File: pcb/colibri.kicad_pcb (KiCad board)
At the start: 2 copper layers, 160 x 94.7 mm, 91 parts

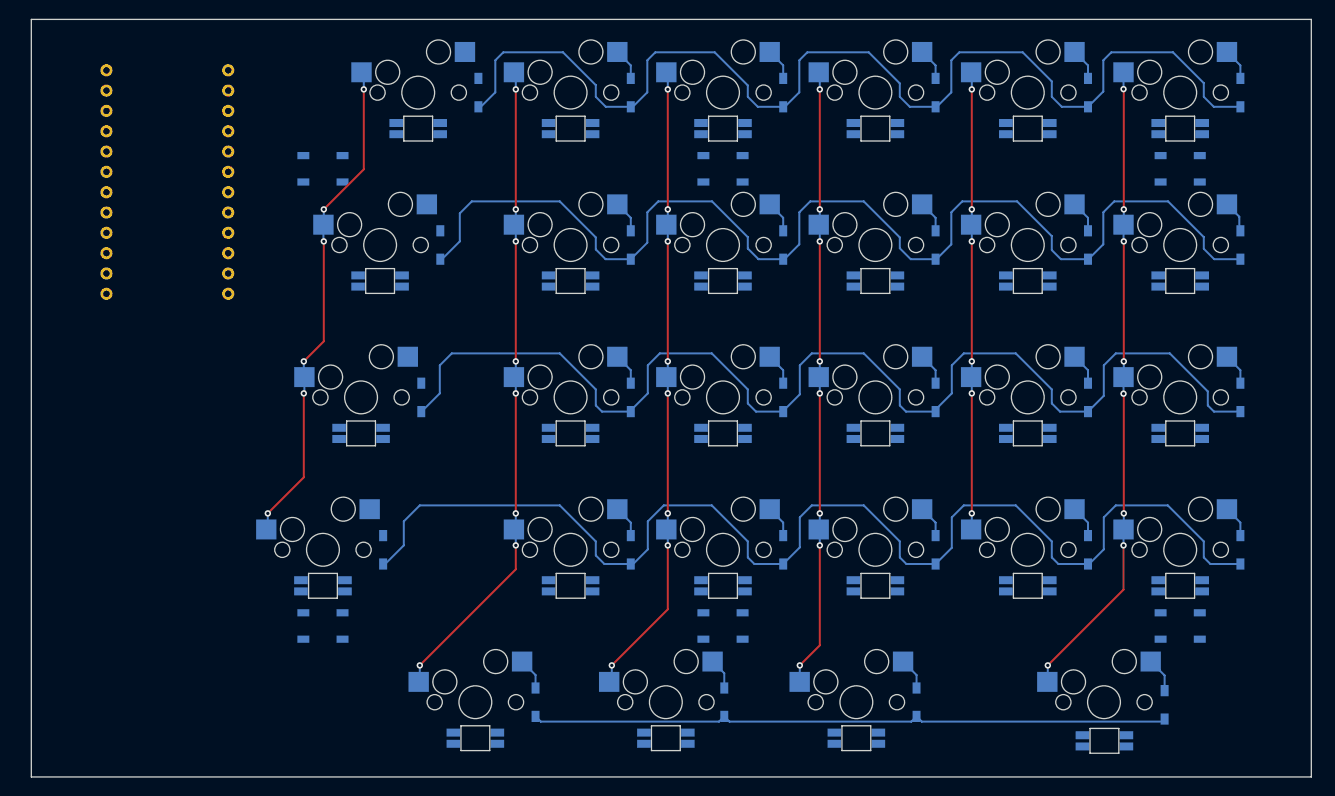
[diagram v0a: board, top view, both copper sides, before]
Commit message: connecting leds
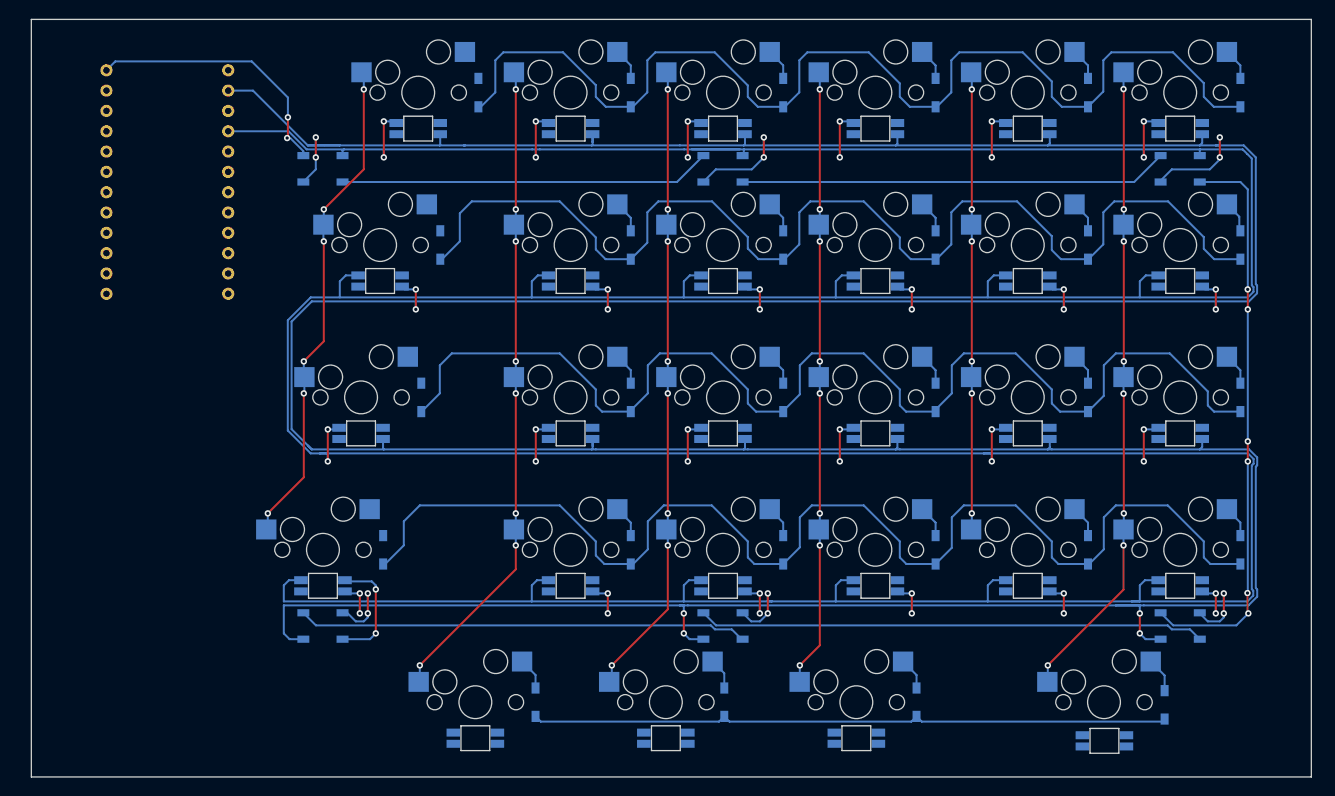
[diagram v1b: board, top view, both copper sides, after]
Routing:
- net lVCC: track 0.00 -> 716.5 mm, vias 0 -> 30
- net lGND: track 0.00 -> 690.2 mm, vias 0 -> 34
- net Net-(lu-3-Pad2): track 0.00 -> 71.7 mm, vias 0 -> 6
- net Net-(lu-5-Pad4): track 0.00 -> 63.4 mm
- net Net-(lu-4-Pad4): track 0.00 -> 56.3 mm
- net Net-(lu-2-Pad2): track 0.00 -> 53.6 mm
- net Net-(lu-1-Pad2): track 0.00 -> 46.5 mm
- net lled: track 0.00 -> 33.4 mm, vias 0 -> 2
- net Net-(lled-19-Pad4): track 0.00 -> 15.3 mm, vias 0 -> 2

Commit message: all leds connected
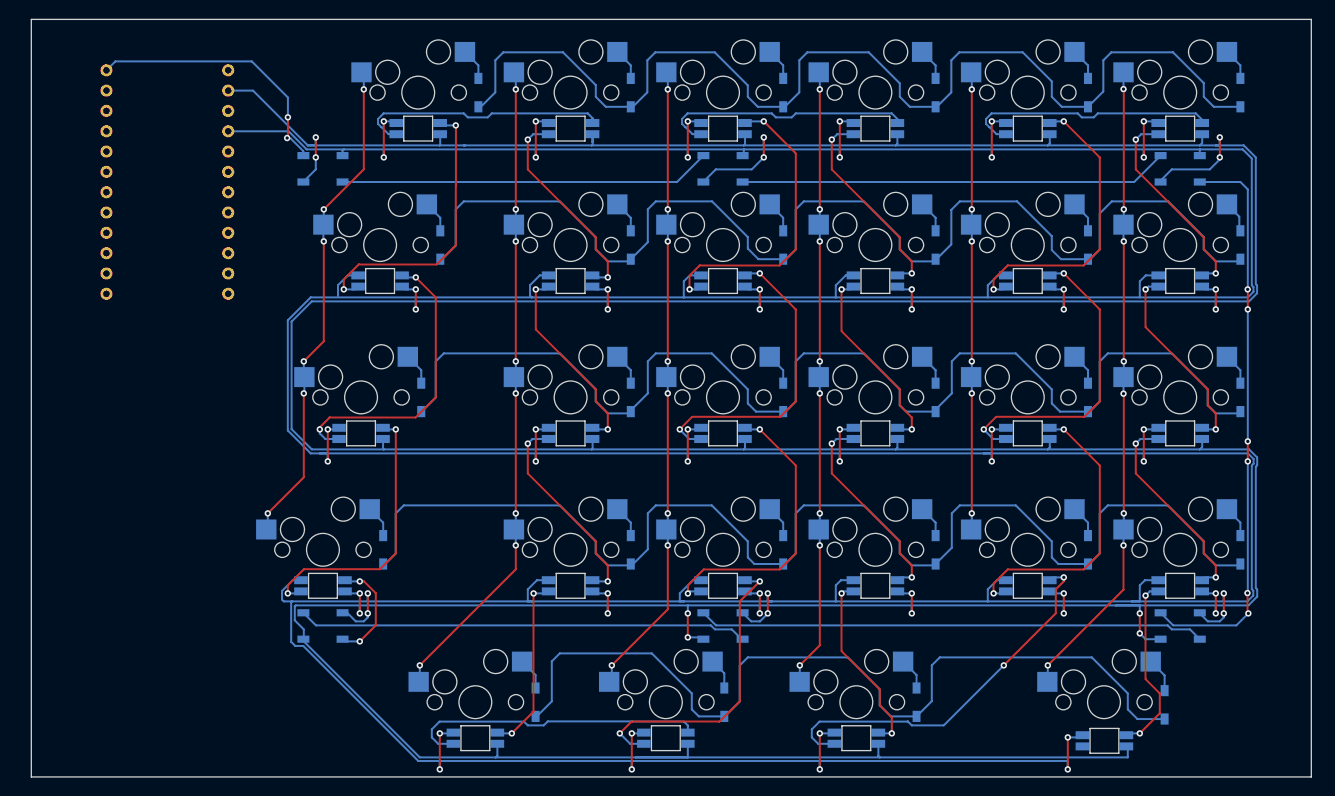
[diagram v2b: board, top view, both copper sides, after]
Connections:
- lled-25 pad 1: unconnected-(lled-25-Pad1) -> lVCC
- lled-25 pad 2: Net-(lled-21-Pad4) -> Net-(lled-26-Pad4)
- lled-25 pad 3: unconnected-(lled-25-Pad3) -> lGND
- lled-26 pad 1: Net-(lled-26-Pad1) -> lVCC
- lled-26 pad 2: Net-(lled-26-Pad2) -> Net-(lled-21-Pad4)
- lled-26 pad 3: unconnected-(lled-26-Pad3) -> lGND
- lled-26 pad 4: Net-(lled-22-Pad2) -> Net-(lled-26-Pad4)
- lled-27 pad 1: Net-(lled-26-Pad1) -> lVCC
- lled-27 pad 4: Net-(lled-26-Pad2) -> Net-(lled-22-Pad2)
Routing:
- net lVCC: track 716.5 -> 841.6 mm, vias 30 -> 38
- net lGND: track 690.2 -> 798.4 mm
- net Net-(lled-27-Pad2): track 0.00 -> 47.4 mm, vias 0 -> 2
- net Net-(lled-15-Pad2): track 0.00 -> 38.6 mm, vias 0 -> 2
- net Net-(lled-11-Pad4): track 0.00 -> 38.6 mm, vias 0 -> 2
- net Net-(lled-26-Pad4): track 0.00 -> 37.9 mm
- net Net-(lled-21-Pad4): track 0.00 -> 37.9 mm, vias 0 -> 2
- net Net-(lled-3-Pad4): track 0.00 -> 37.2 mm, vias 0 -> 2
- net Net-(lled-13-Pad2): track 0.00 -> 37.0 mm, vias 0 -> 2
- net Net-(lled-15-Pad4): track 0.00 -> 36.9 mm, vias 0 -> 2
- net Net-(lled-11-Pad2): track 0.00 -> 36.7 mm, vias 0 -> 2
- net Net-(lled-17-Pad4): track 0.00 -> 36.3 mm, vias 0 -> 2
- net Net-(lled-1-Pad4): track 0.00 -> 35.1 mm, vias 0 -> 2
- net Net-(lled-13-Pad4): track 0.00 -> 34.4 mm, vias 0 -> 2
- net Net-(lled-5-Pad2): track 0.00 -> 32.1 mm
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
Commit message: all keys connected
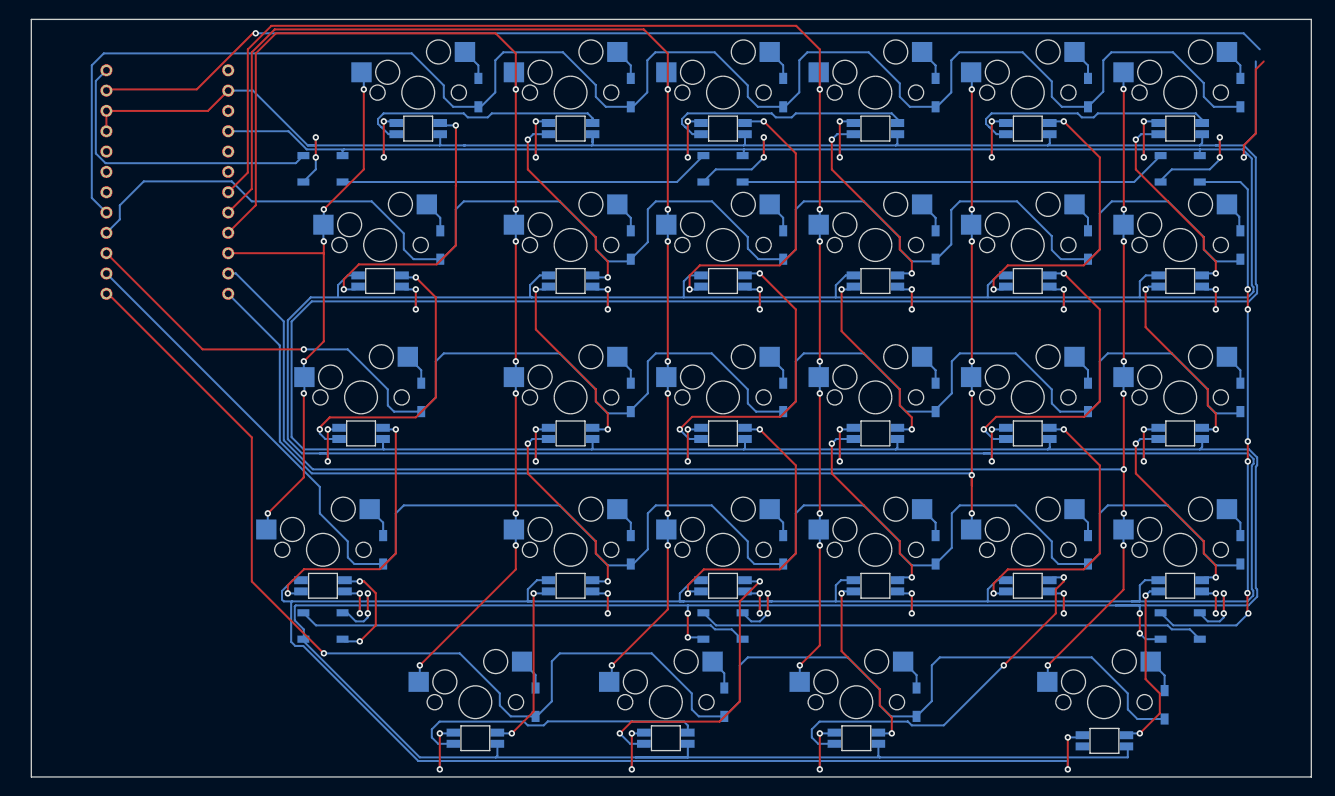
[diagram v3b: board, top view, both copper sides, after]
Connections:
- pro-micro1 pad 11: lrow1 -> lrow3
- pro-micro1 pad 12: lrow0 -> lrow4
- pro-micro1 pad 13: lcol0 -> lcol4
- pro-micro1 pad 14: lcol1 -> lcol5
- pro-micro1 pad 15: lcol2 -> lcol0
- pro-micro1 pad 16: lcol3 -> lcol1
- pro-micro1 pad 17: lcol4 -> lcol2
- pro-micro1 pad 18: lcol5 -> lcol3
- pro-micro1 pad 8: lrow4 -> lrow0
- pro-micro1 pad 9: lrow3 -> lrow1
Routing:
- net ldata: track 0.00 -> 148.0 mm, vias 0 -> 1
- net lcol5: track 80.0 -> 210.4 mm, vias 8 -> 9
- net lcol4: track 56.6 -> 167.3 mm, vias 6 -> 7
- net lcol3: track 76.3 -> 174.1 mm
- net lrow4: track 109.0 -> 195.9 mm, vias 0 -> 1
- net lcol2: track 77.5 -> 157.7 mm
- net lrow0: track 139.0 -> 210.7 mm
- net lcol1: track 79.4 -> 142.3 mm
- net lrow3: track 155.2 -> 207.9 mm
- net lrow1: track 146.2 -> 196.8 mm
- net lrow2: track 149.9 -> 198.6 mm, vias 0 -> 1
- net lGND: track 798.4 -> 828.9 mm
- net lVCC: track 841.6 -> 855.9 mm, vias 38 -> 39
- net lcol0: track 61.6 -> 73.5 mm
- net lled: track 33.4 -> 37.8 mm, vias 2 -> 0

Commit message: added some M2 mounting holes
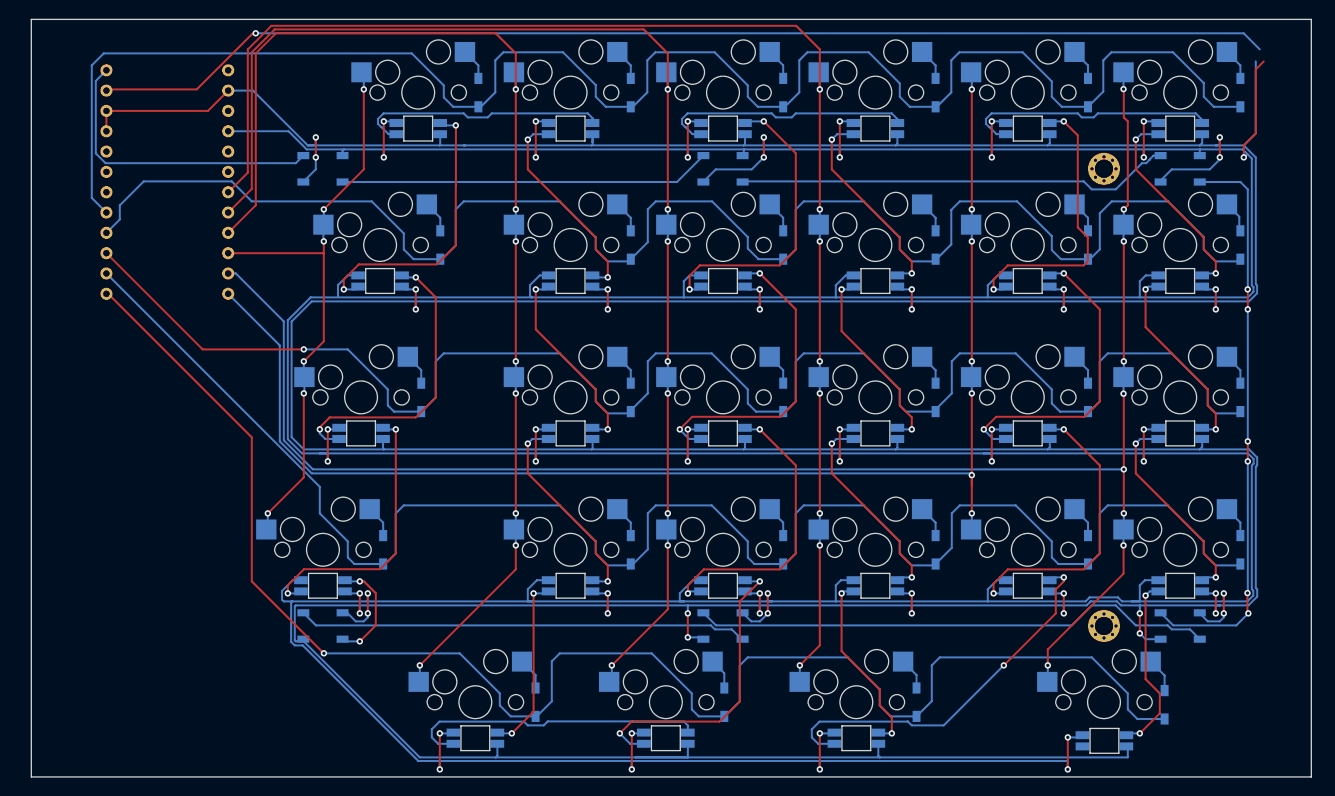
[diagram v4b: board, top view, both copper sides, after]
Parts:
- added Ref**: Val**, kbd:M2_HOLE_v3, F.Cu at (154.5, 116.1)
- added Ref**: Val**, kbd:M2_HOLE_v3, F.Cu at (154.5, 58.9)
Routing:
- net Net-(lu-5-Pad4): track 63.4 -> 65.5 mm
- net Net-(lled-11-Pad2): track 36.7 -> 35.4 mm
- net lGND: track 828.9 -> 827.8 mm
- net Net-(lu-2-Pad2): track 53.6 -> 54.5 mm

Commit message: board size
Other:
- board size 160 x 94.7 mm -> 160 x 95.2 mm
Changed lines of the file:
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@@
     )
   )
-  (gr_rect (start 20.440307 40.249403) (end 180.440307 134.945879) (layer "Edge.Cuts") (width 0.1) (fill none))
+  (gr_line (start 178.575 135.125) (end 18.575 135.125) (layer "Edge.Cuts") (width 0.1))
+  (gr_line (start 178.575 39.875) (end 18.575 39.875) (layer "Edge.Cuts") (width 0.1))
+  (gr_line (start 18.575 39.875) (end 18.575 135.125) (layer "Edge.Cuts") (width 0.1))
+  (gr_line (start 178.575 39.875) (end 178.575 135.125) (layer "Edge.Cuts") (width 0.1))
   (segment (start 91 49.924905) (end 91 48.462452) (width 0.25) (layer "B.Cu") (net 1))
   (segment (start 73.175 51.175) (end 72 50) (width 0.25) (layer "B.Cu") (net 1))

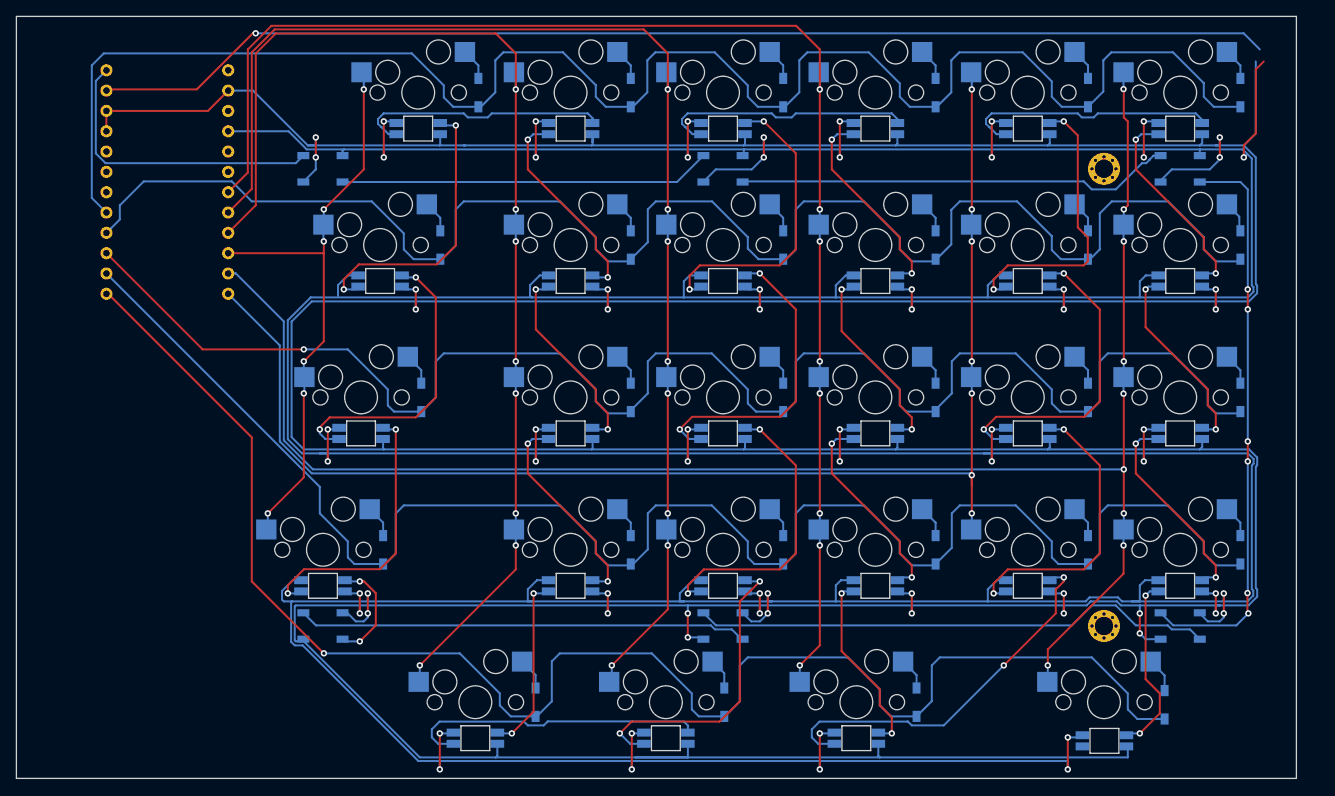
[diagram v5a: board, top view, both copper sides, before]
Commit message: TRRS jack in place
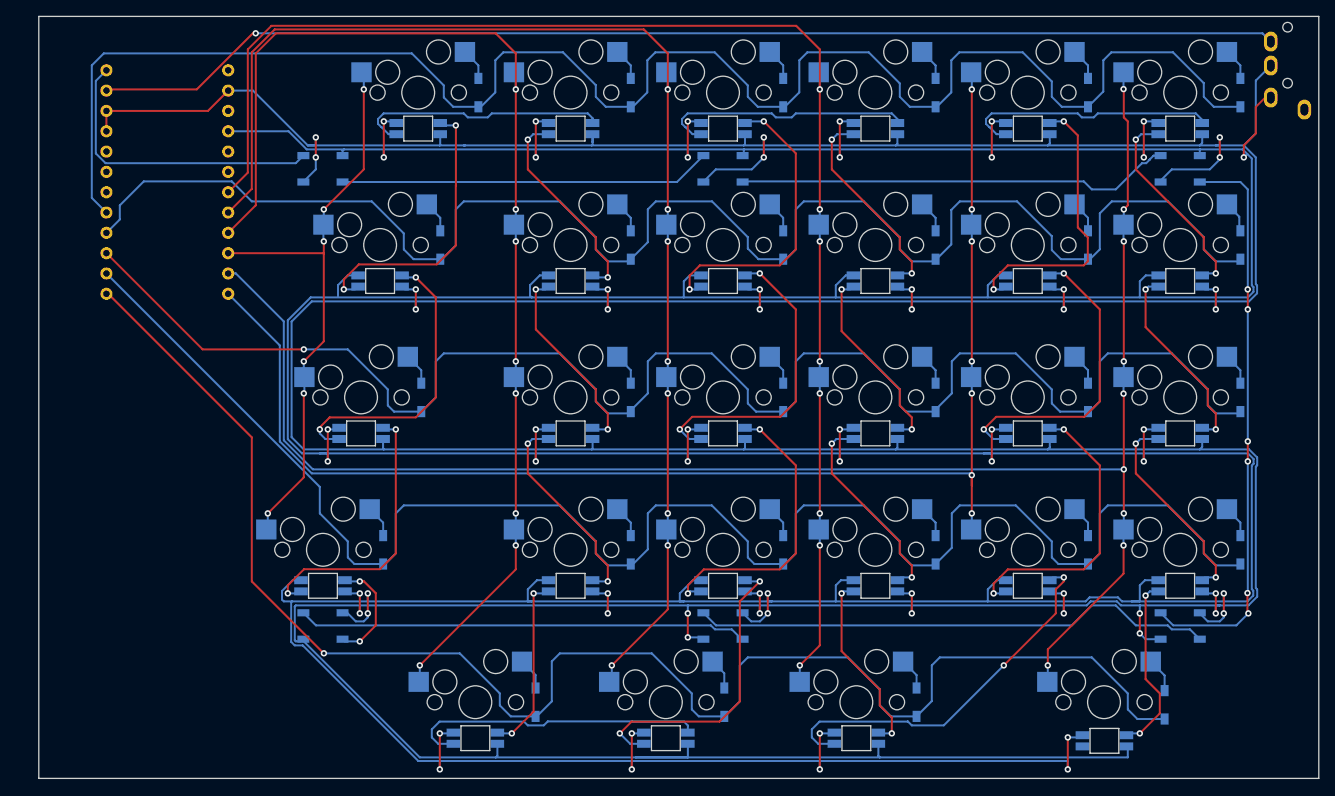
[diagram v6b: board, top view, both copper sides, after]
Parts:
- removed Ref** (x2): Val**, kbd:M2_HOLE_v3
- added ljack-1: MJ-4PP-9, kbd:MJ-4PP-9_1side, B.Cu at (177.5, 39.7)
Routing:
- net lVCC: track 856.3 -> 851.8 mm
- net ldata: track 148.0 -> 148.7 mm
